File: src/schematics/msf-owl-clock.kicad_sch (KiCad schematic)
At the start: 12 parts, among them U001 BC805M

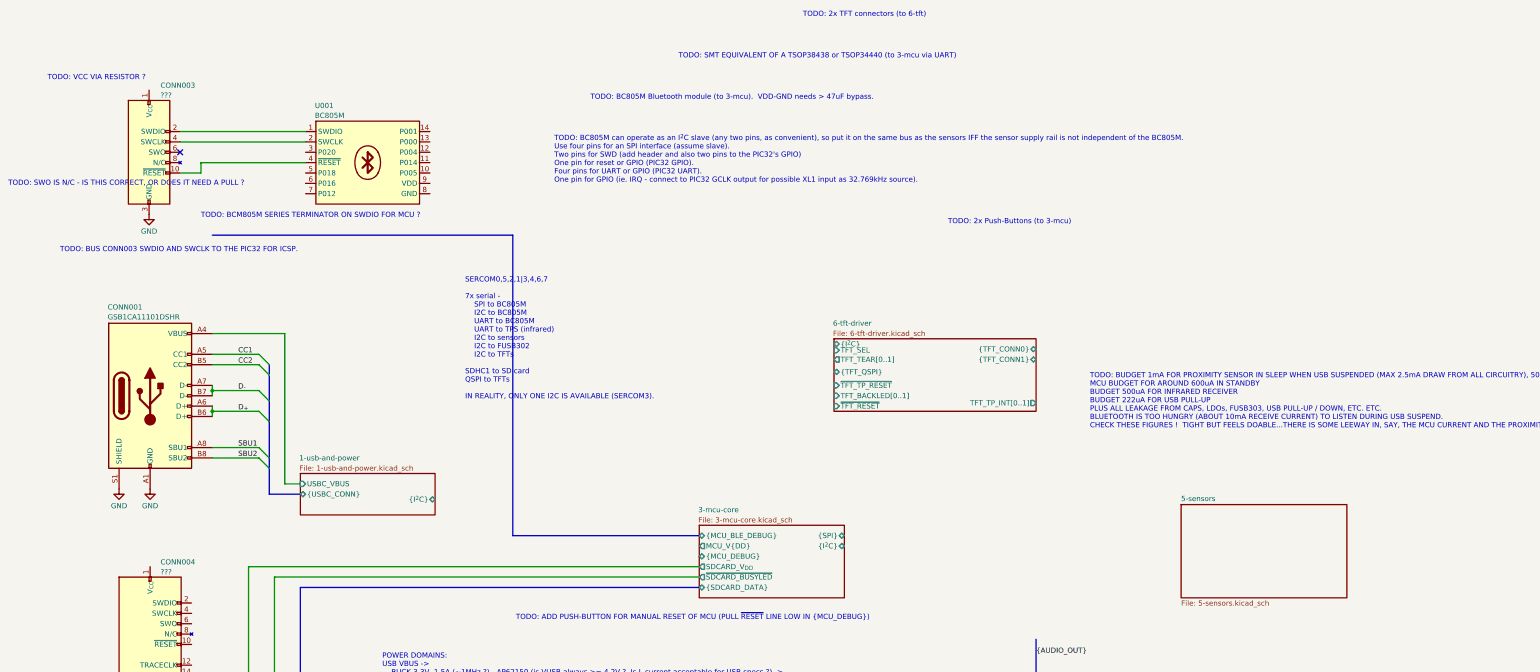
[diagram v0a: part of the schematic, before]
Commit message: Further MCU elaboration and pin mapping.
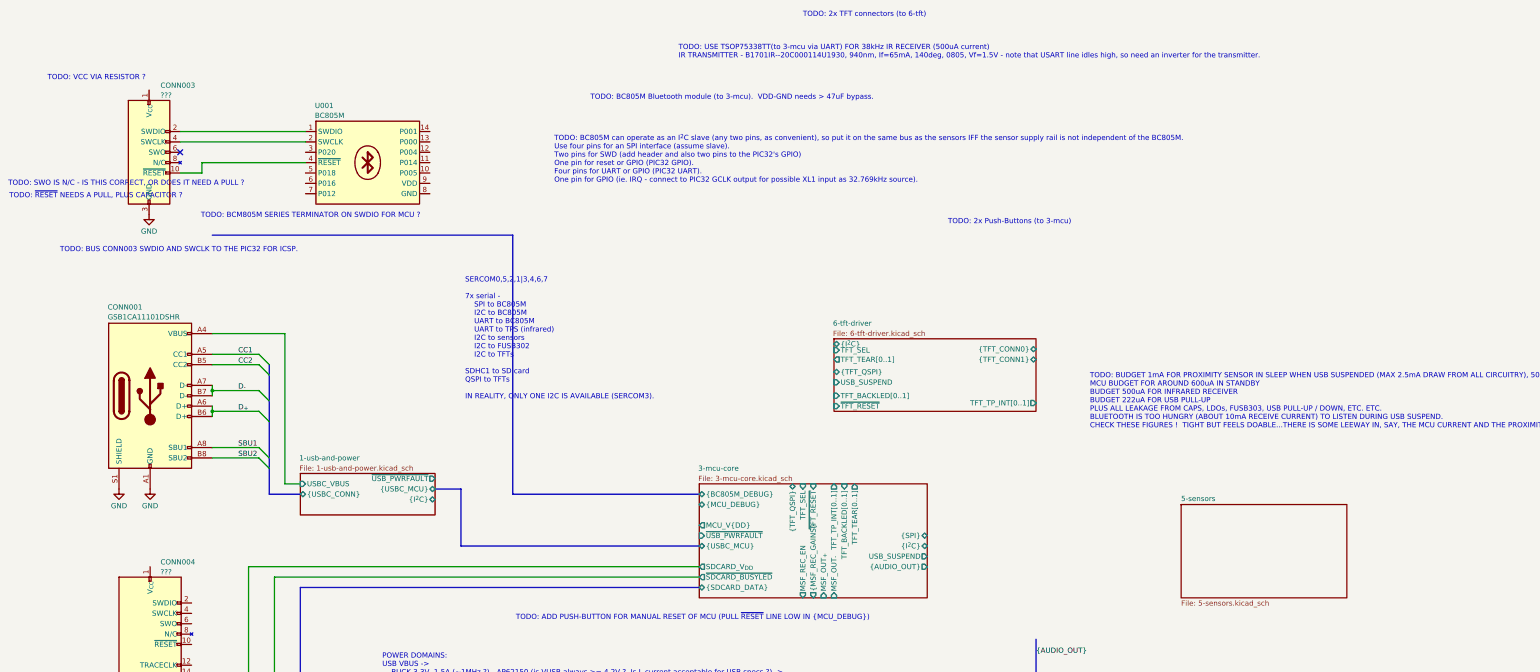
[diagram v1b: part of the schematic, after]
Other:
- sheet 1-usb-and-power ports: added {USBC_MCU}, ~{USB_PWRFAULT}; removed none
- sheet 3-mcu-core ports: added MSF_OUT_{+}, MSF_OUT_{-}, MSF_REC_EN, TFT_BACKLED[0..1], TFT_SEL, TFT_TEAR[0..1], TFT_TP_INT[0..1], USB_SUSPEND, {AUDIO_OUT}, {BC805M_DEBUG}, {MSF_REC_GAINS}, {TFT_QSPI}, {USBC_MCU}, ~{TFT_RESET}, ~{USB_PWRFAULT}; removed {MCU_BLE_DEBUG}
- sheet 6-tft-driver ports: added USB_SUSPEND; removed ~{TFT_TP_RESET}
- note added: "TODO: USE TSOP75338TT(to 3-mcu via UART) FOR 38kHz IR RECEIVER (500uA current) IR TRANSMITTER - B1701IR--20C000114U1930, 940nm, If=65mA, 140deg, 0805, Vf=1.5V - note that USART line idles high, so need an inverter for the transmitter."
- note added: "TODO: ~{RESET} NEEDS A PULL, PLUS CAPACITOR ?"
- note removed: "TODO: SMT EQUIVALENT OF A TSOP38438 or TSOP34440 (to 3-mcu via UART)"
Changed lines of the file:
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@@
     (stroke (width 0) (type default))
   )
-  (bus (pts (xy 172.72 132.08) (xy 127 132.08))
+  (bus (pts (xy 172.72 121.92) (xy 127 121.92))
     (stroke (width 0) (type default))
   )
@@
     (stroke (width 0) (type default))
   )
+  (bus (pts (xy 114.3 120.65) (xy 107.95 120.65))
+    (stroke (width 0) (type default))
+  )
+  (bus (pts (xy 172.72 134.62) (xy 114.3 134.62))
+    (stroke (width 0) (type default))
+  )
   (wire (pts (xy 68.58 200.66) (xy 68.58 198.12))
     (stroke (width 0) (type default))
@@
     (stroke (width 0) (type default))
   )
+  (bus (pts (xy 114.3 134.62) (xy 114.3 120.65))
+    (stroke (width 0) (type default))
+  )
   (bus (pts (xy 67.31 99.06) (xy 67.31 104.14))
     (stroke (width 0) (type default))
@@
     (stroke (width 0) (type default))
   )
-  (bus (pts (xy 127 58.42) (xy 127 132.08))
+  (bus (pts (xy 127 58.42) (xy 127 121.92))
     (stroke (width 0) (type default))
   )
@@
     (stroke (width 0) (type default))
   )
-  (wire (pts (xy 50.546 40.64) (xy 50.546 43.18))
+  (wire (pts (xy 50.8 40.64) (xy 50.8 43.18))
     (stroke (width 0) (type default))
   )
@@
     (stroke (width 0) (type default))
   )
-  (wire (pts (xy 50.546 43.18) (xy 45.466 43.18))
+  (wire (pts (xy 50.8 43.18) (xy 45.466 43.18))
     (stroke (width 0) (type default))
   )
@@
     (stroke (width 0) (type default))
   )
-  (wire (pts (xy 50.546 40.64) (xy 76.2 40.64))
+  (wire (pts (xy 50.8 40.64) (xy 76.2 40.64))
     (stroke (width 0) (type default))
   )
@@
     (effects (font (size 1.27 1.27)) (justify left bottom))
   )
-  (text "TODO: SMT EQUIVALENT OF A TSOP38438 or TSOP34440 (to 3-mcu via UART)"
+  (text "TODO: USE TSOP75338TT(to 3-mcu via UART) FOR 38kHz IR RECEIVER (500uA current)\nIR TRANSMITTER - B1701IR--20C000114U1930, 940nm, If=65mA, 140deg, 0805, Vf=1.5V - note that USART line idles high, so need an inverter for the transmitter."
     (at 167.64 15.24 0)
     (effects (font (size 1.27 1.27)) (justify left bottom))
@@
   (text "TODO: BC805M Bluetooth module (to 3-mcu).  VDD-GND needs > 47uF bypass."
     (at 146.05 25.4 0)
+    (effects (font (size 1.27 1.27)) (justify left bottom))
+  )
+  (text "TODO: ~{RESET} NEEDS A PULL, PLUS CAPACITOR ?" (at 3.556 49.53 0)
     (effects (font (size 1.27 1.27)) (justify left bottom))
   )
@@
       (effects (font (size 1.27 1.27)) (justify left))
     )
-    (pin "~{TFT_TP_RESET}" input (at 205.74 95.25 180)
-      (effects (font (size 1.27 1.27)) (justify left))
-    )
     (pin "{TFT_QSPI}" bidirectional (at 205.74 91.948 180)
       (effects (font (size 1.27 1.27)) (justify left))
@@
     (pin "{TFT_CONN1}" bidirectional (at 255.27 88.9 0)
       (effects (font (size 1.27 1.27)) (justify right))
+    )
+    (pin "USB_SUSPEND" input (at 205.74 94.488 180)
+      (effects (font (size 1.27 1.27)) (justify left))
     )
     (instances
@@
       (effects (font (size 1.27 1.27)) (justify left))
     )
+    (pin "{USBC_MCU}" bidirectional (at 107.95 120.65 0)
+      (effects (font (size 1.27 1.27)) (justify right))
+    )
+    (pin "~{USB_PWRFAULT}" output (at 107.95 118.11 0)
+      (effects (font (size 1.27 1.27)) (justify right))
+    )
     (instances
       (project "msf-owl-clock"
@@
     )
   )
-  (sheet (at 172.72 129.54) (size 35.56 17.78)
+  (sheet (at 172.72 119.38) (size 55.88 27.94)
     (stroke (width 0.1524) (type solid))
     (fill (color 0 0 0 0.0000))
-    (property "Sheetname" "3-mcu-core" (at 172.466 126.492 0)
+    (property "Sheetname" "3-mcu-core" (at 172.466 116.332 0)
       (effects (font (size 1.27 1.27)) (justify left bottom))
     )
-    (property "Sheetfile" "3-mcu-core.kicad_sch" (at 172.466 127.508 0)
+    (property "Sheetfile" "3-mcu-core.kicad_sch" (at 172.466 117.348 0)
       (effects (font (size 1.27 1.27)) (justify left top))
     )
@@
       (effects (font (size 1.27 1.27)) (justify left))
     )
-    (pin "{SPI}" bidirectional (at 208.28 132.08 0)
-      (effects (font (size 1.27 1.27)) (justify right))
-    )
-    (pin "{I^{2}C}" bidirectional (at 208.28 134.62 0)
-      (effects (font (size 1.27 1.27)) (justify right))
-    )
-    (pin "MCU_V{DD}" output (at 172.72 134.62 180)
-      (effects (font (size 1.27 1.27)) (justify left))
-    )
-    (pin "{MCU_DEBUG}" bidirectional (at 172.72 137.16 180)
-      (effects (font (size 1.27 1.27)) (justify left))
-    )
-    (pin "{MCU_BLE_DEBUG}" bidirectional (at 172.72 132.08 180)
-      (effects (font (size 1.27 1.27)) (justify left))
-    )
-    (instances
+    (pin "{SPI}" bidirectional (at 228.6 132.08 0)
+      (effects (font (size 1.27 1.27)) (justify right))
+    )
+    (pin "{I^{2}C}" bidirectional (at 228.6 134.62 0)
+      (effects (font (size 1.27 1.27)) (justify right))
+    )
+    (pin "MCU_V{DD}" output (at 172.72 129.54 180)
+      (effects (font (size 1.27 1.27)) (justify left))
+    )
+    (pin "{MCU_DEBUG}" bidirectional (at 172.72 124.46 180)
+      (effects (font (size 1.27 1.27)) (justify left))
+    )
+    (pin "{BC805M_DEBUG}" bidirectional (at 172.72 121.92 180)
+      (effects (font (size 1.27 1.27)) (justify left))
+    )
+    (pin "TFT_TEAR[0..1]" output (at 210.82 119.38 90)
+      (effects (font (size 1.27 1.27)) (justify right))
+    )
+    (pin "{TFT_QSPI}" bidirectional (at 195.58 119.38 90)
+      (effects (font (size 1.27 1.27)) (justify right))
+    )
+    (pin "TFT_SEL" input (at 198.12 119.38 90)
+      (effects (font (size 1.27 1.27)) (justify right))
+    )
+    (pin "~{TFT_RESET}" input (at 200.66 119.38 90)
+      (effects (font (size 1.27 1.27)) (justify right))
+    )
+    (pin "TFT_TP_INT[0..1]" output (at 205.74 119.38 90)
+      (effects (font (size 1.27 1.27)) (justify right))
+    )
+    (pin "TFT_BACKLED[0..1]" input (at 208.28 119.38 90)
+      (effects (font (size 1.27 1.27)) (justify right))
+    )
+    (pin "{USBC_MCU}" bidirectional (at 172.72 134.62 180)
+      (effects (font (size 1.27 1.27)) (justify left))
+    )
+    (pin "USB_SUSPEND" output (at 228.6 137.16 0)
+      (effects (font (size 1.27 1.27)) (justify right))
+    )
+    (pin "~{USB_PWRFAULT}" input (at 172.72 132.08 180)
+      (effects (font (size 1.27 1.27)) (justify left))
+    )
+    (pin "{MSF_REC_GAINS}" output (at 200.66 147.32 270)
+      (effects (font (size 1.27 1.27)) (justify left))
+    )
+    (pin "MSF_OUT_{+}" input (at 203.2 147.32 270)
+      (effects (font (size 1.27 1.27)) (justify left))
+    )
+    (pin "MSF_OUT_{-}" input (at 205.74 147.32 270)
+      (effects (font (size 1.27 1.27)) (justify left))
+    )
+    (pin "MSF_REC_EN" output (at 198.12 147.32 270)
+      (effects (font (size 1.27 1.27)) (justify left))
+    )
+    (pin "{AUDIO_OUT}" output (at 228.6 139.7 0)
+      (effects (font (size 1.27 1.27)) (justify right))
+    )
+    (instances

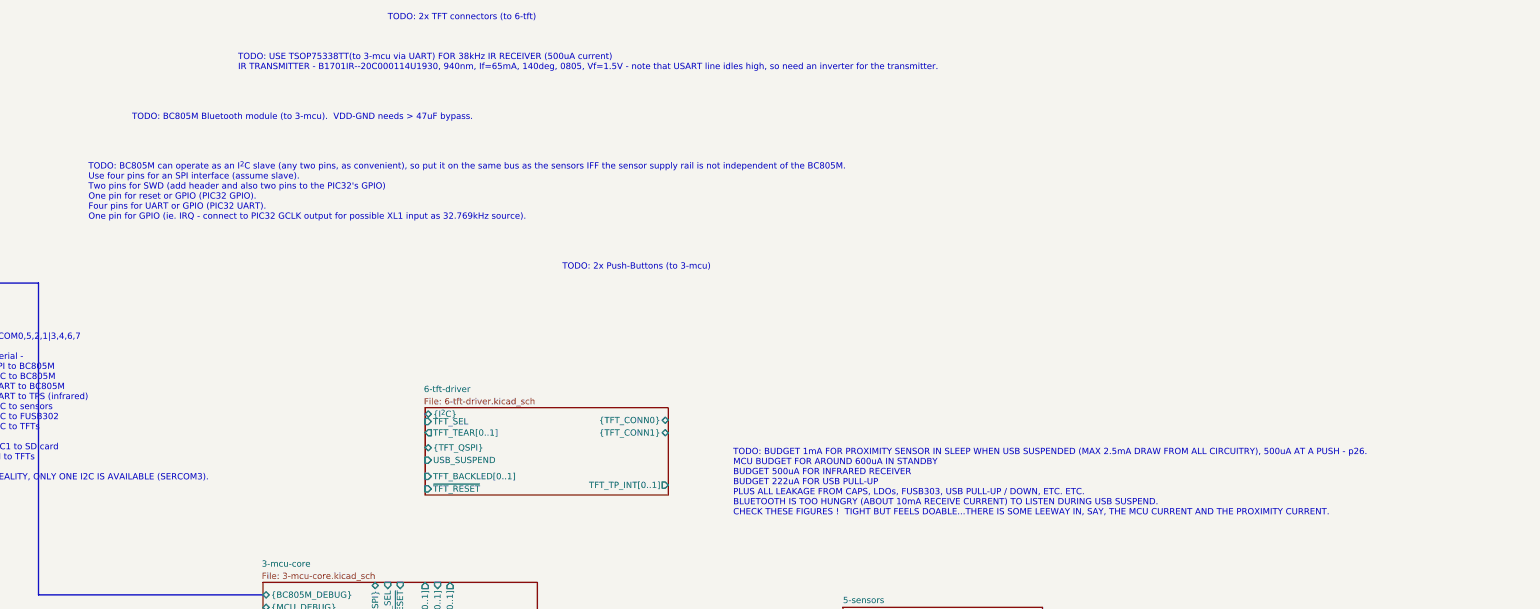
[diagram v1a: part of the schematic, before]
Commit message: Further elaboration of the design, particularly around the power budget.  It's clear that the USB Suspend current of 2.5mA won't be met, mainly due to the DPS1133 power switch's quiescent current.  This is a nice part worth keeping though as it contains OVP, OCP and reverse voltage protection all in one, up to 24V maximum input.
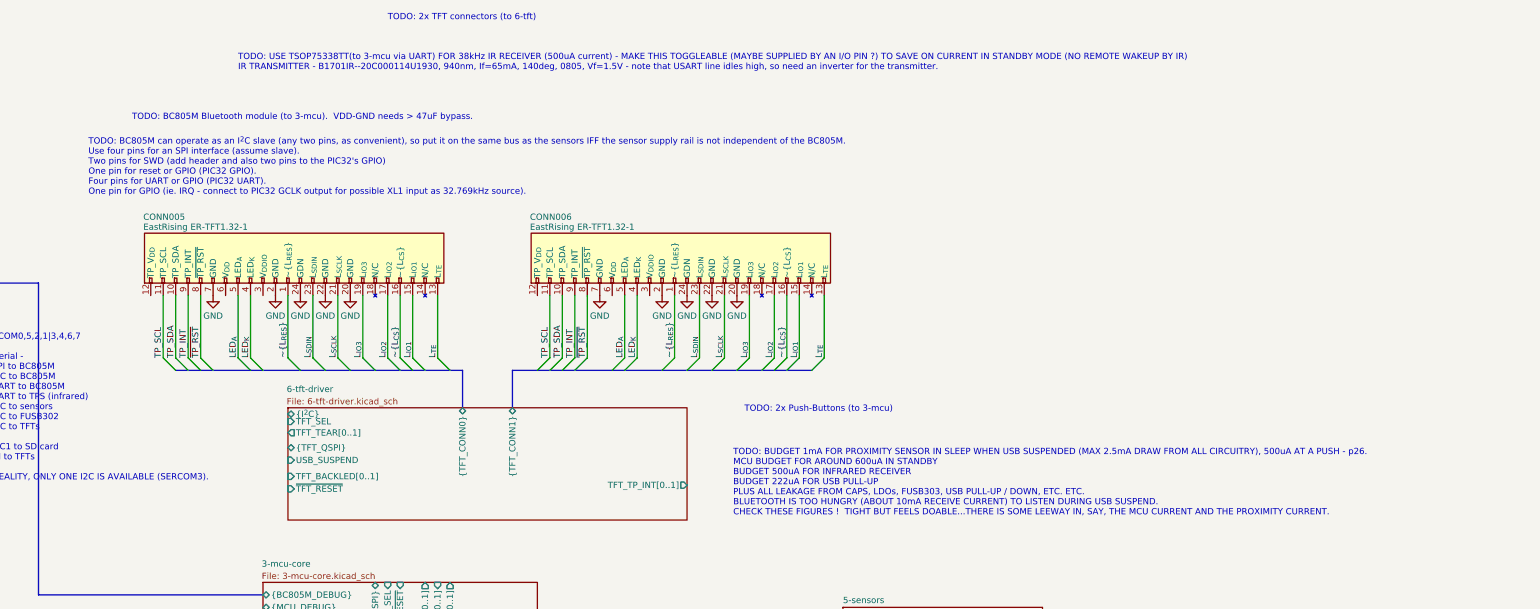
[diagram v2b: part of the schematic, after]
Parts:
- added CONN005, CONN006: EastRising ER-TFT1.32-1, symbol restall-manufacturer-eastrising:ER-TFT1.32-1-reversed-direct-layout
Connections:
- net GND: now also CONN005.2 (GND), CONN005.20 (GND), CONN005.22 (GND), CONN005.24 (GDN), CONN005.7 (GND), CONN006.2 (GND), CONN006.20 (GND), CONN006.22 (GND), CONN006.24 (GDN), CONN006.7 (GND)
- new net LED_{A}: CONN005.5 (LED_{A}), CONN006.5 (LED_{A})
- new net LED_{K}: CONN005.4 (LED_{K}), CONN006.4 (LED_{K})
- new net L_{IO1}: CONN005.15 (L_{IO1}), CONN006.15 (L_{IO1})
- new net L_{IO2}: CONN005.17 (L_{IO2}), CONN006.17 (L_{IO2})
- new net L_{IO3}: CONN005.19 (L_{IO3}), CONN006.19 (L_{IO3})
- new net L_{SCLK}: CONN005.21 (L_{SCLK}), CONN006.21 (L_{SCLK})
- new net L_{SDIN}: CONN005.23 (L_{SDIN}), CONN006.23 (L_{SDIN})
- new net L_{TE}: CONN005.13 (L_{TE}), CONN006.13 (L_{TE})
- new net TP_INT: CONN005.9 (TP_INT), CONN006.9 (TP_INT)
- new net TP_SCL: CONN005.11 (TP_SCL), CONN006.11 (TP_SCL)
- new net TP_SDA: CONN005.10 (TP_SDA), CONN006.10 (TP_SDA)
- new net ~{L_{CS}}: CONN005.16 (~{L_{CS}}), CONN006.16 (~{L_{CS}})
- new net ~{L_{RES}}: CONN005.1 (~{L_{RES}}), CONN006.1 (~{L_{RES}})
- new net ~{TP_RST}: CONN005.8 (~{TP_RST}), CONN006.8 (~{TP_RST})
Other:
- note added: "TODO: USE TSOP75338TT(to 3-mcu via UART) FOR 38kHz IR RECEIVER (500uA current) - MAKE THIS TOGGLEABLE (MAYBE SUPPLIED BY AN I/O PIN ?) TO SAVE ON CURRENT IN STANDBY MODE (NO REMOTE WAKEUP BY IR) IR TRANSMITTER - B1701IR--20C000114U1930, 940nm, If=65mA, 140deg, 0805, Vf=1.5V - note that USART line idles high, so need an inverter for the transmitter."
- note removed: "TODO: USE TSOP75338TT(to 3-mcu via UART) FOR 38kHz IR RECEIVER (500uA current) IR TRANSMITTER - B1701IR--20C000114U1930, 940nm, If=65mA, 140deg, 0805, Vf=1.5V - note that USART line idles high, so need an inverter for the transmitter."
